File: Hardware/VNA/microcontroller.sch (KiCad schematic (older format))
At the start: 0 parts

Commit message: prelim schematic capture complete
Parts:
- added C58, C62, C69, C71: 1u, symbol Device:C
- added C59, C63, C64, C66, C68, C70, C72, C73: 100n, symbol Device:C
- added C60, C61: 10p, symbol Device:C
- added C65, C67: 1u, symbol Device:CP
- added D11, D12, D13, D14: LED, symbol Device:LED
- added D15: LED_ARGB, symbol Device:LED_ARGB
- added FB5: Bead, symbol VNA_Symbols:Ferrite_Bead_PWR
- added R49: DNP, symbol Device:R
- added R50: 10K, symbol Device:R
- added R51: 0R0, symbol Device:R
- added R52, R53, R54, R55: 470R, symbol Device:R
- added SW1, SW2, SW3: SW_Push, symbol Switch:SW_Push
- added U16: STM32F373RCTx, Package_QFP:LQFP-64_10x10mm_P0.5mm, symbol MCU_ST_STM32F3:STM32F373RCTx
- added U17: AT25SF081-SSHD-X, Package_SO:SOIC-8_3.9x4.9mm_P1.27mm, symbol Memory_Flash:AT25SF081-SSHD-X
- added Y1: 8MHz, symbol Device:Crystal
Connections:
- net labels added: 3V3, 3V3A, ATTEN_CLK, ATTEN_DATA, ATTEN_LE, BOOT0, FILTER_SW_1, FILTER_SW_2, FLASH_SPI_MISO, FLASH_SPI_MOSI, FLASH_SPI_SCK, FLASH_nCS, FLASH_nHOLD, FLASH_nWP, GND, INPUT_SW_1, INPUT_SW_2, MAX2871_CE, MAX2871_LD, MAX2871_LE, MAX2871_RF_EN, MAX2871_SPI_MISO, MAX2871_SPI_MOSI, MAX2871_SPI_SCK, PA_PWRDN, SCL, SDA, SDADC_AIN4P, SDADC_AIN5P, SDADC_AIN6P, SDADC_AIN7P, SDADC_AIN8P, STATUS_LED_B, STATUS_LED_G, STATUS_LED_R, SWD_CLK, SWD_IO, USART1_RX, USART1_TX, USB_DM, USB_DP, VDD, VDDA, VREF, nRST
- wire segments 0 -> 191
- no-connect marks 0 -> 8
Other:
- note added: "Debug LEDs"
- note added: "For Testing"
- note added: "HSE"
- note added: "SPI Flash"
- note added: "Status LED"

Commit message: all 3d models created, prelim bom generated
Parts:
- removed D15: LED_ARGB, symbol Device:LED_ARGB
- added D15: LED_RGBA, VNA_Footprints:ARGB_PLCC4_1210_LED, symbol VNA_Symbols:LED_RGBA
- added R56, R57: 0R0, Resistor_SMD:R_0603_1608Metric, symbol Device:R
- added R58: 1K5, Resistor_SMD:R_0603_1608Metric, symbol Device:R
- added TP20, TP21, TP22, TP23, TP24, TP25, TP26, TP27, TP28, TP29, TP30, TP31, TP32, TP33, TP34, TP35, TP36, TP37, TP38, TP39, TP40, TP41, TP42: TP, TestPoint:TestPoint_Pad_D1.0mm, symbol Connector:TestPoint
- C58, C59, C62, C63, C64, C66, C68, C69, C70, C71, C72, C73: footprint (none) -> Capacitor_SMD:C_0603_1608Metric
- C60, C61: footprint (none) -> Capacitor_SMD:C_0402_1005Metric
- C65, C67: footprint (none) -> Capacitor_Tantalum_SMD:CP_EIA-2012-15_AVX-P
- D11, D12, D13, D14: footprint (none) -> LED_SMD:LED_0603_1608Metric
- FB5: footprint (none) -> VNA_Footprints:BEADC1608X95N
- R49, R50, R51, R52, R53, R54, R55: footprint (none) -> Resistor_SMD:R_0603_1608Metric
- SW1, SW2, SW3: footprint (none) -> VNA_Footprints:6mmTactSwitch
- Y1: footprint (none) -> VNA_Footprints:Crystal_SMD_5032-2Pin_5.0x3.2mm
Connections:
- wire segments 191 -> 220
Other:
- note added: "Test Points"

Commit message: More schematic changes + updated functionals
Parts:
- added TP44: TP, TestPoint:TestPoint_Pad_D1.0mm, symbol Connector:TestPoint
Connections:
- net ATTEN_MISO: now reaches U16.48 (PF7)
- net ATTEN_MISO: now also TP27.1
- net ATTEN_DATA renamed ATTEN_MOSI
- net ATTEN_MOSI: now also TP44.1; no longer TP27.1
- no-connect marks 8 -> 7
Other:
- moved on the sheet: C60, C61, R51, TP27, TP28, TP29, TP30, TP31, TP38, TP39, TP40, TP41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

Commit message: first day of layout / routing done
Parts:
- added R64: DNP, Resistor_SMD:R_0603_1608Metric, symbol Device:R
- added R65, R66: 10K, Resistor_SMD:R_0603_1608Metric, symbol Device:R
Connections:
- net GND: now also R65.2, R66.2
- net VDD: now also C69.1, C70.1, C71.1, C72.1, R64.1; no longer C65.1, C66.1, C67.1, C68.1
- net VDDA: now also C65.1, C66.1, C67.1, C68.1; no longer C69.1, C70.1, C71.1, C72.1
- net nRST: now also R64.2
- net at SW1.2, U16.38 (PC7): now also R66.1
- net at SW2.2, U16.40 (PC9): now also R65.1
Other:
- moved on the sheet: C63, R49, R50, SW1, SW2, SW3

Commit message: more routing progress
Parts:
- removed TP29, TP30, TP39, TP40, TP42: TP, TestPoint:TestPoint_Pad_D1.0mm, symbol Connector:TestPoint
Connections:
- net ATTEN_CLK: now also U16.3 (PC14); no longer U16.52 (PC11)
- net ATTEN_MOSI: now also U16.2 (PC13); no longer U16.51 (PC10)
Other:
- moved on the sheet: TP23, TP24, TP25, TP26, TP27, TP28, TP31, TP35, TP36, TP37, TP38, TP41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

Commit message: no unrouted nets!
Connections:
- net ATTEN_MISO: now also U16.52 (PC11); no longer U16.48 (PF7)
- net at R66.1, U16.38 (PC7): now also SW2.2; no longer SW1.2
- net at R65.1, U16.40 (PC9): now also SW1.2; no longer SW2.2
- no-connect marks 7 -> 6
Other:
- moved on the sheet: R65, R66, SW1, SW2
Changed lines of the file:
@@
 Wire Wire Line
 	3000 5300 3000 5350
-$Comp
-L MCU_ST_STM32F3:STM32F373RCTx U16
-U 1 1 5CB87045
-P 3000 3400
-F 0 "U16" H 2450 5150 50  0000 C CNN
-F 1 "STM32F373RCTx" V 3000 3450 50  0000 C CNN
-F 2 "Package_QFP:LQFP-64_10x10mm_P0.5mm" H 2400 1600 50  0001 R CNN
-F 3 "http://www.st.com/st-web-ui/static/active/en/resource/technical/document/datasheet/DM00046749.pdf" H 3000 3400 50  0001 C CNN
-	1    3000 3400
-	1    0    0    -1
-$EndComp
 Text HLabel 3750 4000 2    50   Input ~ 10
 SDADC_AIN6P
@@
 L Switch:SW_Push SW1
 U 1 1 5CED3E76
-P 900 4100
-F 0 "SW1" H 1000 4200 50  0000 C CNN
-F 1 "SW_Push" H 900 4050 50  0000 C CNN
-F 2 "VNA_Footprints:6mmTactSwitch" H 900 4300 50  0001 C CNN
-F 3 "~" H 900 4300 50  0001 C CNN
-	1    900  4100
+P 900 4500
+F 0 "SW1" H 1000 4600 50  0000 C CNN
+F 1 "SW_Push" H 900 4450 50  0000 C CNN
+F 2 "VNA_Footprints:6mmTactSwitch" H 900 4700 50  0001 C CNN
+F 3 "~" H 900 4700 50  0001 C CNN
+	1    900  4500
 	1    0    0    -1
 $EndComp
@@
 L Switch:SW_Push SW2
 U 1 1 5CEF0A38
-P 900 4500
-F 0 "SW2" H 1000 4600 50  0000 C CNN
-F 1 "SW_Push" H 900 4450 50  0000 C CNN
-F 2 "VNA_Footprints:6mmTactSwitch" H 900 4700 50  0001 C CNN
-F 3 "~" H 900 4700 50  0001 C CNN
-	1    900  4500
+P 900 4100
+F 0 "SW2" H 1000 4200 50  0000 C CNN
+F 1 "SW_Push" H 900 4050 50  0000 C CNN
+F 2 "VNA_Footprints:6mmTactSwitch" H 900 4300 50  0001 C CNN
+F 3 "~" H 900 4300 50  0001 C CNN
+	1    900  4100
 	1    0    0    -1
 $EndComp
@@
 	650  4500 650  4550
 Wire Wire Line
-	1100 4500 1250 4500
+	1100 4500 1200 4500
 Wire Wire Line
 	1100 4100 1250 4100
@@
 	1250 4100 1250 4300
 Wire Wire Line
-	1250 4300 1550 4300
+	1250 4300 1500 4300
 Text Notes 650  3900 0    100  ~ 20
 For Testing
@@
 Wire Wire Line
 	8650 4350 8550 4350
-Text HLabel 2250 2800 0    50   Input ~ 10
+Text HLabel 2250 4700 0    50   Input ~ 10
 ATTEN_MISO
 Wire Wire Line
@@
 Text HLabel 1850 1000 1    50   Input ~ 10
 3V3
+Wire Wire Line
+	2250 4900 2300 4900
+Wire Wire Line
+	2250 5000 2300 5000
+Wire Wire Line
+	2300 4800 2250 4800
+NoConn ~ 2300 4600
+$Comp
+L MCU_ST_STM32F3:STM32F373RCTx U16
+U 1 1 5CB87045
+P 3000 3400
+F 0 "U16" H 2450 5150 50  0000 C CNN
+F 1 "STM32F373RCTx" V 3000 3450 50  0000 C CNN
+F 2 "Package_QFP:LQFP-64_10x10mm_P0.5mm" H 2400 1600 50  0001 R CNN
+F 3 "http://www.st.com/st-web-ui/static/active/en/resource/technical/document/datasheet/DM00046749.pdf" H 3000 3400 50  0001 C CNN
+	1    3000 3400
+	1    0    0    -1
+$EndComp
+Wire Wire Line
+	2300 4700 2250 4700
+Wire Wire Line
+	1500 4950 1500 4900
+$Comp
+L power:GND #PWR0126
+U 1 1 5CE704F2
+P 1500 4950
+F 0 "#PWR0126" H 1500 4700 50  0001 C CNN
+F 1 "GND" H 1505 4777 50  0000 C CNN
+F 2 "" H 1500 4950 50  0001 C CNN
+F 3 "" H 1500 4950 50  0001 C CNN
+	1    1500 4950
+	1    0    0    -1
+$EndComp
+Wire Wire Line
+	1200 4950 1200 4900
+$Comp
+L power:GND #PWR0125
+U 1 1 5CE610E8
+P 1200 4950
+F 0 "#PWR0125" H 1200 4700 50  0001 C CNN
+F 1 "GND" H 1205 4777 50  0000 C CNN
+F 2 "" H 1200 4950 50  0001 C CNN
+F 3 "" H 1200 4950 50  0001 C CNN
+	1    1200 4950
+	1    0    0    -1
+$EndComp
+Wire Wire Line
+	1500 4600 1500 4300
+Wire Wire Line
+	1200 4600 1200 4500
+$Comp
+L Device:R R65
+U 1 1 5CE27EFC
+P 1200 4750
+F 0 "R65" H 1270 4796 50  0000 L CNN
+F 1 "10K" H 1270 4705 50  0000 L CNN
+F 2 "Resistor_SMD:R_0603_1608Metric" V 1130 4750 50  0001 C CNN
+F 3 "~" H 1200 4750 50  0001 C CNN
+	1    1200 4750
+	1    0    0    -1
+$EndComp
 $Comp
 L Device:R R66
 U 1 1 5CE2733D
-P 1550 4750
-F 0 "R66" H 1620 4796 50  0000 L CNN
-F 1 "10K" H 1620 4705 50  0000 L CNN
-F 2 "Resistor_SMD:R_0603_1608Metric" V 1480 4750 50  0001 C CNN
-F 3 "~" H 1550 4750 50  0001 C CNN
-	1    1550 4750
-	1    0    0    -1
-$EndComp
-$Comp
-L Device:R R65
-U 1 1 5CE27EFC
-P 1250 4750
-F 0 "R65" H 1320 4796 50  0000 L CNN
-F 1 "10K" H 1320 4705 50  0000 L CNN
-F 2 "Resistor_SMD:R_0603_1608Metric" V 1180 4750 50  0001 C CNN
-F 3 "~" H 1250 4750 50  0001 C CNN
-	1    1250 4750
-	1    0    0    -1
-$EndComp
-Wire Wire Line
-	1250 4600 1250 4500
-Connection ~ 1250 4500
-Wire Wire Line
-	1250 4500 2300 4500
-Wire Wire Line
-	1550 4600 1550 4300
-Connection ~ 1550 4300
-Wire Wire Line
-	1550 4300 2300 4300
-$Comp
-L power:GND #PWR0125
-U 1 1 5CE610E8
-P 1250 4950
-F 0 "#PWR0125" H 1250 4700 50  0001 C CNN
-F 1 "GND" H 1255 4777 50  0000 C CNN
-F 2 "" H 1250 4950 50  0001 C CNN
-F 3 "" H 1250 4950 50  0001 C CNN
-	1    1250 4950
-	1    0    0    -1
-$EndComp
-Wire Wire Line
-	1250 4950 1250 4900
-$Comp
-L power:GND #PWR0126
-U 1 1 5CE704F2
-P 1550 4950
-F 0 "#PWR0126" H 1550 4700 50  0001 C CNN
-F 1 "GND" H 1555 4777 50  0000 C CNN
-F 2 "" H 1550 4950 50  0001 C CNN
-F 3 "" H 1550 4950 50  0001 C CNN
-	1    1550 4950
-	1    0    0    -1
-$EndComp
-Wire Wire Line
-	1550 4950 1550 4900
-Wire Wire Line
-	2250 4900 2300 4900
-Wire Wire Line
-	2250 5000 2300 5000
-NoConn ~ 2300 4700
-Wire Wire Line
-	2300 4800 2250 4800
-NoConn ~ 2300 4600
+P 1500 4750
+F 0 "R66" H 1570 4796 50  0000 L CNN
+F 1 "10K" H 1570 4705 50  0000 L CNN
+F 2 "Resistor_SMD:R_0603_1608Metric" V 1430 4750 50  0001 C CNN
+F 3 "~" H 1500 4750 50  0001 C CNN
+	1    1500 4750
+	1    0    0    -1
+$EndComp
+Connection ~ 1200 4500
+Connection ~ 1500 4300
+Wire Wire Line
+	1200 4500 2300 4500
+Wire Wire Line
+	1500 4300 2300 4300
 $EndSCHEMATC

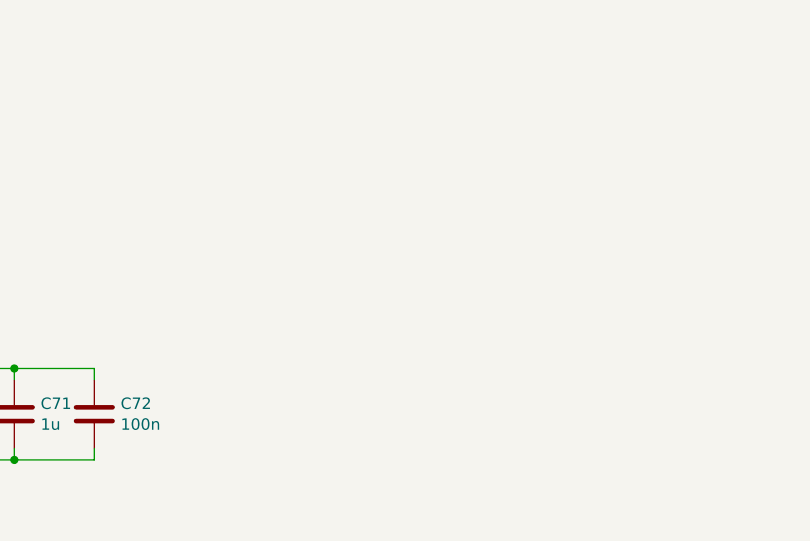
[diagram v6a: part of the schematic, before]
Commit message: Layout done, front and rear panels designed
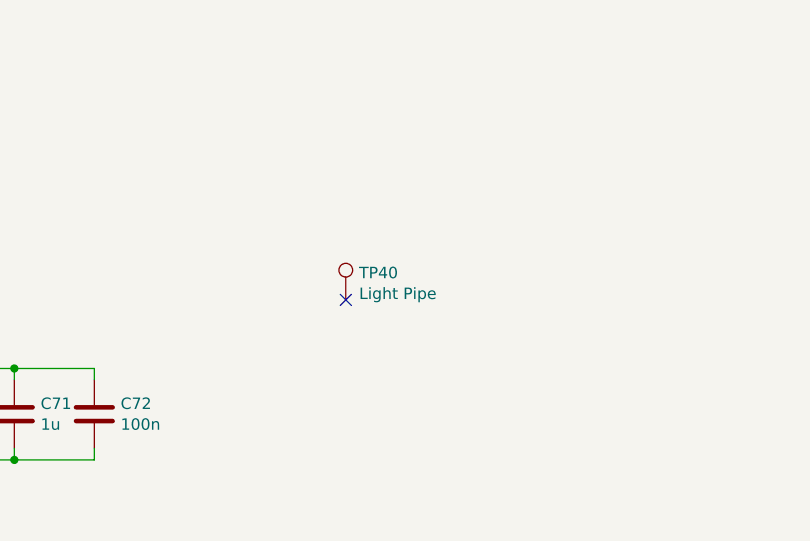
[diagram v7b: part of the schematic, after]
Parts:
- added TP40: Light Pipe, VNA_Footprints:SLP3-150-150-F, symbol Connector:TestPoint
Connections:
- no-connect marks 6 -> 7
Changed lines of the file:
@@
 Wire Wire Line
 	1500 4300 2300 4300
+$Comp
+L Connector:TestPoint TP40
+U 1 1 5CBF934F
+P 6300 6800
+F 0 "TP40" H 6358 6918 50  0000 L CNN
+F 1 "Light Pipe" H 6358 6827 50  0000 L CNN
+F 2 "VNA_Footprints:SLP3-150-150-F" H 6500 6800 50  0001 C CNN
+F 3 "~" H 6500 6800 50  0001 C CNN
+	1    6300 6800
+	1    0    0    -1
+$EndComp
+NoConn ~ 6300 6800
 $EndSCHEMATC

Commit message: Gerbers generated, ready for fab
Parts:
- added TP29: Test2, TestPoint:TestPoint_Pad_D1.0mm, symbol Connector:TestPoint
- added TP42: Test1, TestPoint:TestPoint_Pad_D1.0mm, symbol Connector:TestPoint
- added TP45: Test3, TestPoint:TestPoint_Pad_D1.0mm, symbol Connector:TestPoint
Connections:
- net FLASH_SPI_MISO: now also U16.22 (PA6); no longer U16.10 (PC2)
- net FLASH_SPI_MOSI: now also U16.23 (PA7); no longer U16.11 (PC3)
- net FLASH_SPI_SCK: now also U16.21 (PA5); no longer U16.36 (PD8)
- net FLASH_nCS: now also U16.16 (PA2); no longer U16.9 (PC1)
- net FLASH_nHOLD: now also U16.18 (PA3); no longer U16.4 (PC15)
- net FLASH_nWP: now also U16.9 (PC1); no longer U16.8 (PC0)
- net MAX2871_CE: now also U16.4 (PC15); no longer U16.18 (PA3)
- net MAX2871_LD: now also U16.14 (PA0); no longer U16.15 (PA1)
- net MAX2871_LE: now also U16.8 (PC0); no longer U16.14 (PA0)
- net MAX2871_RF_EN: now also U16.15 (PA1); no longer U16.16 (PA2)
- net MAX2871_SPI_MISO: now also U16.10 (PC2); no longer U16.22 (PA6)
- net MAX2871_SPI_MOSI: now also U16.11 (PC3); no longer U16.23 (PA7)
- net MAX2871_SPI_SCK: now also U16.36 (PD8); no longer U16.21 (PA5)
- net at U16.41 (PA8): now also TP42.1
- net at U16.42 (PA9): now also TP29.1
- net at U16.43 (PA10): now also TP45.1
- no-connect marks 7 -> 4
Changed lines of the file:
@@
 Text Label 2250 4200 2    50   ~ 10
 STATUS_LED_R
-Text Label 2250 5100 2    50   ~ 10
+Text Label 3750 2600 0    50   ~ 10
 FLASH_nHOLD
 Wire Wire Line
 	2300 5100 2250 5100
-Text Label 2250 3600 2    50   ~ 10
+Text Label 2250 3700 2    50   ~ 10
 FLASH_nWP
 Wire Wire Line
 	2300 3600 2250 3600
-Text Label 2250 3700 2    50   ~ 10
+Text Label 3750 2500 0    50   ~ 10
 FLASH_nCS
 Wire Wire Line
 	2300 3700 2250 3700
-Text Label 2250 3400 2    50   ~ 10
+Text Label 3750 2800 0    50   ~ 10
 FLASH_SPI_SCK
 Text HLabel 3750 4700 2    50   Input ~ 10
@@
 Wire Wire Line
 	2300 4000 2250 4000
-Text HLabel 3750 3000 2    50   Input ~ 10
+Text HLabel 2250 3900 0    50   Input ~ 10
 MAX2871_SPI_MOSI
-Text HLabel 3750 2900 2    50   Input ~ 10
+Text HLabel 2250 3800 0    50   Input ~ 10
 MAX2871_SPI_MISO
-Text HLabel 3750 2800 2    50   Input ~ 10
+Text HLabel 2250 3400 0    50   Input ~ 10
 MAX2871_SPI_SCK
 Wire Wire Line
@@
 Wire Wire Line
 	3700 2800 3750 2800
-Text Label 2250 3900 2    50   ~ 10
+Text Label 3750 3000 0    50   ~ 10
 FLASH_SPI_MOSI
-Text Label 2250 3800 2    50   ~ 10
+Text Label 3750 2900 0    50   ~ 10
 FLASH_SPI_MISO
 Wire Wire Line
@@
 Text HLabel 2250 3100 0    50   Input ~ 10
 SDADC_AIN7P
-Text HLabel 3750 2600 2    50   Input ~ 10
+Text HLabel 2250 5100 0    50   Input ~ 10
 MAX2871_CE
 Wire Wire Line
@@
 Wire Wire Line
 	3700 2300 3750 2300
-Text HLabel 3750 2500 2    50   Input ~ 10
+Text HLabel 3750 2400 2    50   Input ~ 10
 MAX2871_RF_EN
-Text HLabel 3750 2400 2    50   Input ~ 10
+Text HLabel 3750 2300 2    50   Input ~ 10
 MAX2871_LD
-Text HLabel 3750 2300 2    50   Input ~ 10
+Text HLabel 2250 3600 0    50   Input ~ 10
 MAX2871_LE
 Wire Wire Line
@@
 $EndComp
 NoConn ~ 2300 2700
-NoConn ~ 3700 3100
-NoConn ~ 3700 3200
-NoConn ~ 3700 3300
 $Comp
 L Device:CP C65
@@
 	2300 4800 2250 4800
 NoConn ~ 2300 4600
+Wire Wire Line
+	2300 4700 2250 4700
+Wire Wire Line
+	1500 4950 1500 4900
+$Comp
+L power:GND #PWR0126
+U 1 1 5CE704F2
+P 1500 4950
+F 0 "#PWR0126" H 1500 4700 50  0001 C CNN
+F 1 "GND" H 1505 4777 50  0000 C CNN
+F 2 "" H 1500 4950 50  0001 C CNN
+F 3 "" H 1500 4950 50  0001 C CNN
+	1    1500 4950
+	1    0    0    -1
+$EndComp
+Wire Wire Line
+	1200 4950 1200 4900
+$Comp
+L power:GND #PWR0125
+U 1 1 5CE610E8
+P 1200 4950
+F 0 "#PWR0125" H 1200 4700 50  0001 C CNN
+F 1 "GND" H 1205 4777 50  0000 C CNN
+F 2 "" H 1200 4950 50  0001 C CNN
+F 3 "" H 1200 4950 50  0001 C CNN
+	1    1200 4950
+	1    0    0    -1
+$EndComp
+Wire Wire Line
+	1500 4600 1500 4300
+Wire Wire Line
+	1200 4600 1200 4500
+$Comp
+L Device:R R65
+U 1 1 5CE27EFC
+P 1200 4750
+F 0 "R65" H 1270 4796 50  0000 L CNN
+F 1 "10K" H 1270 4705 50  0000 L CNN
+F 2 "Resistor_SMD:R_0603_1608Metric" V 1130 4750 50  0001 C CNN
+F 3 "~" H 1200 4750 50  0001 C CNN
+	1    1200 4750
+	1    0    0    -1
+$EndComp
+$Comp
+L Device:R R66
+U 1 1 5CE2733D
+P 1500 4750
+F 0 "R66" H 1570 4796 50  0000 L CNN
+F 1 "10K" H 1570 4705 50  0000 L CNN
+F 2 "Resistor_SMD:R_0603_1608Metric" V 1430 4750 50  0001 C CNN
+F 3 "~" H 1500 4750 50  0001 C CNN
+	1    1500 4750
+	1    0    0    -1
+$EndComp
+Connection ~ 1200 4500
+Connection ~ 1500 4300
+Wire Wire Line
+	1200 4500 2300 4500
+Wire Wire Line
+	1500 4300 2300 4300
+$Comp
+L Connector:TestPoint TP40
+U 1 1 5CBF934F
+P 6300 6800
+F 0 "TP40" H 6358 6918 50  0000 L CNN
+F 1 "Light Pipe" H 6358 6827 50  0000 L CNN
+F 2 "VNA_Footprints:SLP3-150-150-F" H 6500 6800 50  0001 C CNN
+F 3 "~" H 6500 6800 50  0001 C CNN
+	1    6300 6800
+	1    0    0    -1
+$EndComp
+NoConn ~ 6300 6800
 $Comp
 L MCU_ST_STM32F3:STM32F373RCTx U16
@@
 	1    0    0    -1
 $EndComp
-Wire Wire Line
-	2300 4700 2250 4700
-Wire Wire Line
-	1500 4950 1500 4900
-$Comp
-L power:GND #PWR0126
-U 1 1 5CE704F2
-P 1500 4950
-F 0 "#PWR0126" H 1500 4700 50  0001 C CNN
-F 1 "GND" H 1505 4777 50  0000 C CNN
-F 2 "" H 1500 4950 50  0001 C CNN
-F 3 "" H 1500 4950 50  0001 C CNN
-	1    1500 4950
-	1    0    0    -1
-$EndComp
-Wire Wire Line
-	1200 4950 1200 4900
-$Comp
-L power:GND #PWR0125
-U 1 1 5CE610E8
-P 1200 4950
-F 0 "#PWR0125" H 1200 4700 50  0001 C CNN
-F 1 "GND" H 1205 4777 50  0000 C CNN
-F 2 "" H 1200 4950 50  0001 C CNN
-F 3 "" H 1200 4950 50  0001 C CNN
-	1    1200 4950
-	1    0    0    -1
-$EndComp
-Wire Wire Line
-	1500 4600 1500 4300
-Wire Wire Line
-	1200 4600 1200 4500
-$Comp
-L Device:R R65
-U 1 1 5CE27EFC
-P 1200 4750
-F 0 "R65" H 1270 4796 50  0000 L CNN
-F 1 "10K" H 1270 4705 50  0000 L CNN
-F 2 "Resistor_SMD:R_0603_1608Metric" V 1130 4750 50  0001 C CNN
-F 3 "~" H 1200 4750 50  0001 C CNN
-	1    1200 4750
-	1    0    0    -1
-$EndComp
-$Comp
-L Device:R R66
-U 1 1 5CE2733D
-P 1500 4750
-F 0 "R66" H 1570 4796 50  0000 L CNN
-F 1 "10K" H 1570 4705 50  0000 L CNN
-F 2 "Resistor_SMD:R_0603_1608Metric" V 1430 4750 50  0001 C CNN
-F 3 "~" H 1500 4750 50  0001 C CNN
-	1    1500 4750
-	1    0    0    -1
-$EndComp
-Connection ~ 1200 4500
-Connection ~ 1500 4300
-Wire Wire Line
-	1200 4500 2300 4500
-Wire Wire Line
-	1500 4300 2300 4300
-$Comp
-L Connector:TestPoint TP40
-U 1 1 5CBF934F
-P 6300 6800
-F 0 "TP40" H 6358 6918 50  0000 L CNN
-F 1 "Light Pipe" H 6358 6827 50  0000 L CNN
-F 2 "VNA_Footprints:SLP3-150-150-F" H 6500 6800 50  0001 C CNN
-F 3 "~" H 6500 6800 50  0001 C CNN
-	1    6300 6800
-	1    0    0    -1
-$EndComp
-NoConn ~ 6300 6800
+$Comp
+L Connector:TestPoint TP45
+U 1 1 5CBAC71B
+P 4900 3300
+F 0 "TP45" V 4854 3488 50  0000 L CNN
+F 1 "Test3" V 4945 3488 50  0000 L CNN
+F 2 "TestPoint:TestPoint_Pad_D1.0mm" H 5100 3300 50  0001 C CNN
+F 3 "~" H 5100 3300 50  0001 C CNN
+	1    4900 3300
+	0    1    1    0
+$EndComp
+Wire Wire Line
+	3700 3300 4900 3300
+Wire Wire Line
+	3700 3200 3900 3200
+$Comp
+L Connector:TestPoint TP29
+U 1 1 5CBCBE24
+P 3900 3200
+F 0 "TP29" V 3854 3388 50  0000 L CNN
+F 1 "Test2" V 3945 3388 50  0000 L CNN
+F 2 "TestPoint:TestPoint_Pad_D1.0mm" H 4100 3200 50  0001 C CNN
+F 3 "~" H 4100 3200 50  0001 C CNN
+	1    3900 3200
+	0    1    1    0
+$EndComp
+Wire Wire Line
+	3700 3100 4900 3100
+$Comp
+L Connector:TestPoint TP42
+U 1 1 5CBDB702
+P 4900 3100
+F 0 "TP42" V 4854 3288 50  0000 L CNN
+F 1 "Test1" V 4945 3288 50  0000 L CNN
+F 2 "TestPoint:TestPoint_Pad_D1.0mm" H 5100 3100 50  0001 C CNN
+F 3 "~" H 5100 3100 50  0001 C CNN
+	1    4900 3100
+	0    1    1    0
+$EndComp
 $EndSCHEMATC
